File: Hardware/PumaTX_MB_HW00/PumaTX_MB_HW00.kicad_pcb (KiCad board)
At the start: 2 copper layers, 107 parts, among them J100 FH12A-26S-0.5SH_55_, J101 FH12-12S-0.5SH_55_, J102 500334-0160, J103 500334-0160, J104 692122030100, J105 53398-0667, J300 U.FL-R-SMT-1_40_, J410 U.FL-R-SMT-1_40_, M130 Motor_DC, M140 Fan, Q130 ZXMN3B01F, Q140 ZXMN3B01F, Q200 UMH3NTN, Q201 UMH3NTN, U200 CP2105-F01-GMR, U300 ESP32-PICO-D4, U400 ESP32-PICO-D4, U402 E28-2G4M27S, U410 SX1280, U500 BQ24075RGTR, U510 MIC5528-3.3YMT-T5, U520 MIC5528-3.3YMT-T5, U530 MIC5528-3.3YMT-T5, Y410 NX2016SA-52MHZ-EXS00A-CS06016

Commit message: Generated BOM and changed 2 capa footprints
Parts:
- C350, C450: footprint Capacitor_SMD:C_0402_1005Metric -> Capacitor_SMD:C_0603_1608Metric
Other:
- board outline added: 216 x 107.5 mm
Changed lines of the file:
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@@
     )
   )
-  (footprint "Capacitor_SMD:C_0402_1005Metric" (layer "F.Cu")
+  (footprint "Capacitor_SMD:C_0603_1608Metric" (layer "F.Cu")
     (at 145.52 80.08)
-    (descr "Capacitor SMD 0402 (1005 Metric), square (rectangular) end terminal, IPC_7351 nominal, (Body size source: IPC-SM-782 page 76, https://www.pcb-3d.com/wordpress/wp-content/uploads/ipc-sm-782a_amendment_1_and_2.pdf), generated with kicad-footprint-generator")
-    (tags "capacitor")
-    (property "Sheetfile" "PumaTX_MB_HW00.kicad_sch")
-    (property "Sheetname" "")
-    (attr smd)
-    (fp_text reference "C350" (at 0 -1.16) (layer "F.SilkS")
-      (effects (font (size 1 1) (thickness 0.15)))
-    )
-    (fp_text value "100n" (at 0 1.16) (layer "F.Fab")
-      (effects (font (size 1 1) (thickness 0.15)))
-    )
-    (fp_text user "${REFERENCE}" (at 0 0) (layer "F.Fab")
-      (effects (font (size 0.25 0.25) (thickness 0.04)))
-    )
-    (fp_line (start -0.107836 -0.36) (end 0.107836 -0.36) (layer "F.SilkS") (width 0.12))
-    (fp_line (start -0.107836 0.36) (end 0.107836 0.36) (layer "F.SilkS") (width 0.12))
-    (fp_line (start 0.91 -0.46) (end 0.91 0.46) (layer "F.CrtYd") (width 0.05))
-    (fp_line (start -0.91 -0.46) (end 0.91 -0.46) (layer "F.CrtYd") (width 0.05))
-    (fp_line (start 0.91 0.46) (end -0.91 0.46) (layer "F.CrtYd") (width 0.05))
-    (fp_line (start -0.91 0.46) (end -0.91 -0.46) (layer "F.CrtYd") (width 0.05))
-    (fp_line (start -0.5 -0.25) (end 0.5 -0.25) (layer "F.Fab") (width 0.1))
-    (fp_line (start -0.5 0.25) (end -0.5 -0.25) (layer "F.Fab") (width 0.1))
-    (fp_line (start 0.5 -0.25) (end 0.5 0.25) (layer "F.Fab") (width 0.1))
-    (fp_line (start 0.5 0.25) (end -0.5 0.25) (layer "F.Fab") (width 0.1))
-    (pad "1" smd roundrect (at -0.48 0) (size 0.56 0.62) (layers "F.Cu" "F.Paste" "F.Mask") (roundrect_rratio 0.25)
+    (descr "Capacitor SMD 0603 (1608 Metric), square (rectangular) end terminal, IPC_7351 nominal, (Body size source: IPC-SM-782 page 76, https://www.pcb-3d.com/wordpress/wp-content/uploads/ipc-sm-782a_amendment_1_and_2.pdf), generated with kicad-footprint-generator")
+    (tags "capacitor")
+    (property "Sheetfile" "PumaTX_MB_HW00.kicad_sch")
+    (property "Sheetname" "")
+    (attr smd)
+    (fp_text reference "C350" (at 0 -1.43) (layer "F.SilkS")
+      (effects (font (size 1 1) (thickness 0.15)))
+    )
+    (fp_text value "100n" (at 0 1.43) (layer "F.Fab")
+      (effects (font (size 1 1) (thickness 0.15)))
+    )
+    (fp_text user "${REFERENCE}" (at 0 0) (layer "F.Fab")
+      (effects (font (size 0.4 0.4) (thickness 0.06)))
+    )
+    (fp_line (start -0.14058 0.51) (end 0.14058 0.51) (layer "F.SilkS") (width 0.12))
+    (fp_line (start -0.14058 -0.51) (end 0.14058 -0.51) (layer "F.SilkS") (width 0.12))
+    (fp_line (start -1.48 -0.73) (end 1.48 -0.73) (layer "F.CrtYd") (width 0.05))
+    (fp_line (start -1.48 0.73) (end -1.48 -0.73) (layer "F.CrtYd") (width 0.05))
+    (fp_line (start 1.48 0.73) (end -1.48 0.73) (layer "F.CrtYd") (width 0.05))
+    (fp_line (start 1.48 -0.73) (end 1.48 0.73) (layer "F.CrtYd") (width 0.05))
+    (fp_line (start 0.8 0.4) (end -0.8 0.4) (layer "F.Fab") (width 0.1))
+    (fp_line (start -0.8 0.4) (end -0.8 -0.4) (layer "F.Fab") (width 0.1))
+    (fp_line (start -0.8 -0.4) (end 0.8 -0.4) (layer "F.Fab") (width 0.1))
+    (fp_line (start 0.8 -0.4) (end 0.8 0.4) (layer "F.Fab") (width 0.1))
+    (pad "1" smd roundrect (at -0.775 0) (size 0.9 0.95) (layers "F.Cu" "F.Paste" "F.Mask") (roundrect_rratio 0.25)
       (net 2 "+3V3") (pintype "passive"))
-    (pad "2" smd roundrect (at 0.48 0) (size 0.56 0.62) (layers "F.Cu" "F.Paste" "F.Mask") (roundrect_rratio 0.25)
-      (net 1 "GND") (pintype "passive"))
-    (model "${KICAD6_3DMODEL_DIR}/Capacitor_SMD.3dshapes/C_0402_1005Metric.wrl"
+    (pad "2" smd roundrect (at 0.775 0) (size 0.9 0.95) (layers "F.Cu" "F.Paste" "F.Mask") (roundrect_rratio 0.25)
+      (net 1 "GND") (pintype "passive"))
+    (model "${KICAD6_3DMODEL_DIR}/Capacitor_SMD.3dshapes/C_0603_1608Metric.wrl"
       (offset (xyz 0 0 0))
       (scale (xyz 1 1 1))
@@
     )
   )
-  (footprint "Capacitor_SMD:C_0402_1005Metric" (layer "F.Cu")
+  (footprint "Capacitor_SMD:C_0603_1608Metric" (layer "F.Cu")
     (at 142.65 77.47)
-    (descr "Capacitor SMD 0402 (1005 Metric), square (rectangular) end terminal, IPC_7351 nominal, (Body size source: IPC-SM-782 page 76, https://www.pcb-3d.com/wordpress/wp-content/uploads/ipc-sm-782a_amendment_1_and_2.pdf), generated with kicad-footprint-generator")
-    (tags "capacitor")
-    (property "Sheetfile" "PumaTX_MB_HW00.kicad_sch")
-    (property "Sheetname" "")
-    (attr smd)
-    (fp_text reference "C450" (at 0 -1.16) (layer "F.SilkS")
-      (effects (font (size 1 1) (thickness 0.15)))
-    )
-    (fp_text value "100n" (at 0 1.16) (layer "F.Fab")
-      (effects (font (size 1 1) (thickness 0.15)))
-    )
-    (fp_text user "${REFERENCE}" (at 0 0) (layer "F.Fab")
-      (effects (font (size 0.25 0.25) (thickness 0.04)))
-    )
-    (fp_line (start -0.107836 0.36) (end 0.107836 0.36) (layer "F.SilkS") (width 0.12))
-    (fp_line (start -0.107836 -0.36) (end 0.107836 -0.36) (layer "F.SilkS") (width 0.12))
-    (fp_line (start 0.91 -0.46) (end 0.91 0.46) (layer "F.CrtYd") (width 0.05))
-    (fp_line (start 0.91 0.46) (end -0.91 0.46) (layer "F.CrtYd") (width 0.05))
-    (fp_line (start -0.91 -0.46) (end 0.91 -0.46) (layer "F.CrtYd") (width 0.05))
-    (fp_line (start -0.91 0.46) (end -0.91 -0.46) (layer "F.CrtYd") (width 0.05))
-    (fp_line (start -0.5 0.25) (end -0.5 -0.25) (layer "F.Fab") (width 0.1))
-    (fp_line (start -0.5 -0.25) (end 0.5 -0.25) (layer "F.Fab") (width 0.1))
-    (fp_line (start 0.5 -0.25) (end 0.5 0.25) (layer "F.Fab") (width 0.1))
-    (fp_line (start 0.5 0.25) (end -0.5 0.25) (layer "F.Fab") (width 0.1))
-    (pad "1" smd roundrect (at -0.48 0) (size 0.56 0.62) (layers "F.Cu" "F.Paste" "F.Mask") (roundrect_rratio 0.25)
+    (descr "Capacitor SMD 0603 (1608 Metric), square (rectangular) end terminal, IPC_7351 nominal, (Body size source: IPC-SM-782 page 76, https://www.pcb-3d.com/wordpress/wp-content/uploads/ipc-sm-782a_amendment_1_and_2.pdf), generated with kicad-footprint-generator")
+    (tags "capacitor")
+    (property "Sheetfile" "PumaTX_MB_HW00.kicad_sch")
+    (property "Sheetname" "")
+    (attr smd)
+    (fp_text reference "C450" (at 0 -1.43) (layer "F.SilkS")
+      (effects (font (size 1 1) (thickness 0.15)))
+    )
+    (fp_text value "100n" (at 0 1.43) (layer "F.Fab")
+      (effects (font (size 1 1) (thickness 0.15)))
+    )
+    (fp_text user "${REFERENCE}" (at 0 0) (layer "F.Fab")
+      (effects (font (size 0.4 0.4) (thickness 0.06)))
+    )
+    (fp_line (start -0.14058 0.51) (end 0.14058 0.51) (layer "F.SilkS") (width 0.12))
+    (fp_line (start -0.14058 -0.51) (end 0.14058 -0.51) (layer "F.SilkS") (width 0.12))
+    (fp_line (start -1.48 -0.73) (end 1.48 -0.73) (layer "F.CrtYd") (width 0.05))
+    (fp_line (start -1.48 0.73) (end -1.48 -0.73) (layer "F.CrtYd") (width 0.05))
+    (fp_line (start 1.48 -0.73) (end 1.48 0.73) (layer "F.CrtYd") (width 0.05))
+    (fp_line (start 1.48 0.73) (end -1.48 0.73) (layer "F.CrtYd") (width 0.05))
+    (fp_line (start 0.8 -0.4) (end 0.8 0.4) (layer "F.Fab") (width 0.1))
+    (fp_line (start -0.8 -0.4) (end 0.8 -0.4) (layer "F.Fab") (width 0.1))
+    (fp_line (start 0.8 0.4) (end -0.8 0.4) (layer "F.Fab") (width 0.1))
+    (fp_line (start -0.8 0.4) (end -0.8 -0.4) (layer "F.Fab") (width 0.1))
+    (pad "1" smd roundrect (at -0.775 0) (size 0.9 0.95) (layers "F.Cu" "F.Paste" "F.Mask") (roundrect_rratio 0.25)
       (net 40 "-3V3") (pintype "passive"))
-    (pad "2" smd roundrect (at 0.48 0) (size 0.56 0.62) (layers "F.Cu" "F.Paste" "F.Mask") (roundrect_rratio 0.25)
-      (net 1 "GND") (pintype "passive"))
-    (model "${KICAD6_3DMODEL_DIR}/Capacitor_SMD.3dshapes/C_0402_1005Metric.wrl"
+    (pad "2" smd roundrect (at 0.775 0) (size 0.9 0.95) (layers "F.Cu" "F.Paste" "F.Mask") (roundrect_rratio 0.25)
+      (net 1 "GND") (pintype "passive"))
+    (model "${KICAD6_3DMODEL_DIR}/Capacitor_SMD.3dshapes/C_0603_1608Metric.wrl"
       (offset (xyz 0 0 0))
       (scale (xyz 1 1 1))
@@
     )
   )
+  (gr_rect (start 53.5 64.5) (end 269.5 172) (layer "Edge.Cuts") (width 0.1) (fill none))
 )

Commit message: PCB layout is done, routing to go!
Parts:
- M130, U300, U400: moved to B.Cu
- moved ANT400 106.9 mm to (216.5, 43.3)
- moved C101 106.9 mm to (234.5, 63.3)
- moved C102 106.9 mm to (213.4, 83.2)
- moved C103 106.9 mm to (237.4, 63.3)
- moved C110 106.9 mm to (249.5, 78.3)
- moved C120 106.9 mm to (241.5, 75.8)
- moved C200 106.9 mm to (229.2, 39.0)
- moved C201 106.9 mm to (228.6, 34.0)
- moved C202 106.9 mm to (233.2, 34.0)
- moved C203 106.9 mm to (233.2, 36.6)
- moved C301 106.9 mm to (243.2, 57.6)
- moved C303 106.9 mm to (225.7, 91.4)
- moved C304 106.9 mm to (225.7, 93.3)
- moved C306 106.9 mm to (236.2, 39.3)
- moved C307 106.9 mm to (239.0, 39.3)
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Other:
- board size 216 x 107.5 mm -> 130 x 40 mm

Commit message: quick layout update
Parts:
- moved D200 114.8 mm to (115.1, 117.2)
- moved Q140 98.7 mm to (184.7, 115.0)
- moved D130 89.7 mm to (193.2, 112.1)
- moved M140 89.6 mm to (179.6, 114.5)
- moved ANT400 78.3 mm to (190.4, 117.2)
- moved U530 71.9 mm to (193.0, 108.2)
- moved D140 71.8 mm to (174.5, 116.7)
- moved Q130 69.6 mm to (202.9, 108.2)
- moved Y410 62.5 mm to (165.1, 92.6)
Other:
- copper layers 2 -> 4
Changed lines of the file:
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@@
 (kicad_pcb (version 20211014) (generator pcbnew)
   (general
-    (thickness 1.6)
+    (thickness 4.69)
   )
   (paper "A4")
   (layers
     (0 "F.Cu" signal)
+    (1 "In1.Cu" signal)
+    (2 "In2.Cu" signal)
     (31 "B.Cu" signal)
     (32 "B.Adhes" user "B.Adhesive")
@@
   )
   (setup
+    (stackup
+      (layer "F.SilkS" (type "Top Silk Screen"))
+      (layer "F.Paste" (type "Top Solder Paste"))
+      (layer "F.Mask" (type "Top Solder Mask") (thickness 0.01))
+      (layer "F.Cu" (type "copper") (thickness 0.035))
+      (layer "dielectric 1" (type "core") (thickness 1.51) (material "FR4") (epsilon_r 4.5) (loss_tangent 0.02))
+      (layer "In1.Cu" (type "copper") (thickness 0.035))
+      (layer "dielectric 2" (type "prepreg") (thickness 1.51) (material "FR4") (epsilon_r 4.5) (loss_tangent 0.02))
+      (layer "In2.Cu" (type "copper") (thickness 0.035))
+      (layer "dielectric 3" (type "core") (thickness 1.51) (material "FR4") (epsilon_r 4.5) (loss_tangent 0.02))
+      (layer "B.Cu" (type "copper") (thickness 0.035))
+      (layer "B.Mask" (type "Bottom Solder Mask") (thickness 0.01))
+      (layer "B.Paste" (type "Bottom Solder Paste"))
+      (layer "B.SilkS" (type "Bottom Silk Screen"))
+      (copper_finish "None")
+      (dielectric_constraints no)
+    )
     (pad_to_mask_clearance 0)
     (pcbplotparams
@@
   )
   (footprint "Component_lib:S1GHE" (layer "F.Cu")
-    (at 230.39 30.528)
+    (at 193.162 112.1)
     (descr "S1GHE-2")
     (tags "Diode")
@@
   )
   (footprint "Package_TO_SOT_SMD:SOT-23" (layer "F.Cu")
-    (at 224.015 41.865)
+    (at 202.8625 108.15)
     (descr "SOT, 3 Pin (https://www.jedec.org/system/files/docs/to-236h.pdf variant AB), generated with kicad-footprint-generator ipc_gullwing_generator.py")
     (tags "SOT TO_SOT_SMD")
@@
   )
   (footprint "Component_lib:S1GHE" (layer "F.Cu")
-    (at 205.91 52.138)
+    (at 174.491 116.65)
     (descr "S1GHE-2")
     (tags "Diode")
@@
   )
   (footprint "Component_lib:SM02B-SURS-TF" (layer "F.Cu")
-    (at 224.37 36.84)
+    (at 179.6 114.5)
     (property "Sheetfile" "PumaTX_MB_HW00.kicad_sch")
     (property "Sheetname" "")
@@
   )
   (footprint "Component_lib:SON40P120X120X60-7N-D" (layer "F.Cu")
-    (at 228.185 45.54)
+    (at 193 108.25)
     (descr "MIC5528-3.3YMT-T5   6pin")
     (tags "Integrated Circuit")
@@
   )
   (footprint "Package_TO_SOT_SMD:SOT-23" (layer "F.Cu")
-    (at 235.915 30.565)
+    (at 184.65 114.95)
     (descr "SOT, 3 Pin (https://www.jedec.org/system/files/docs/to-236h.pdf variant AB), generated with kicad-footprint-generator ipc_gullwing_generator.py")
     (tags "SOT TO_SOT_SMD")
@@
   )
   (footprint "Component_lib:ANTC3216X140N" (layer "F.Cu")
-    (at 216.525 43.335)
+    (at 190.4 117.15)
     (descr "2450AT18A100E")
     (tags "Antenna")
@@
   )
   (footprint "Component_lib:NX2016SA32MEXS00ACS06465" (layer "F.Cu")
-    (at 211.64 50.91)
+    (at 165.1 92.6)
     (descr "NX2016SA-32M-EXS00A-CS06465-2")
     (tags "Crystal or Oscillator")
@@
   )
   (footprint "Component_lib:SP0503BAHTG" (layer "F.Cu")
-    (at 205.15 46)
+    (at 115.1 117.15)
     (descr "SP0503BAHTG-1")
     (tags "TVS Diode (Uni-directional)")

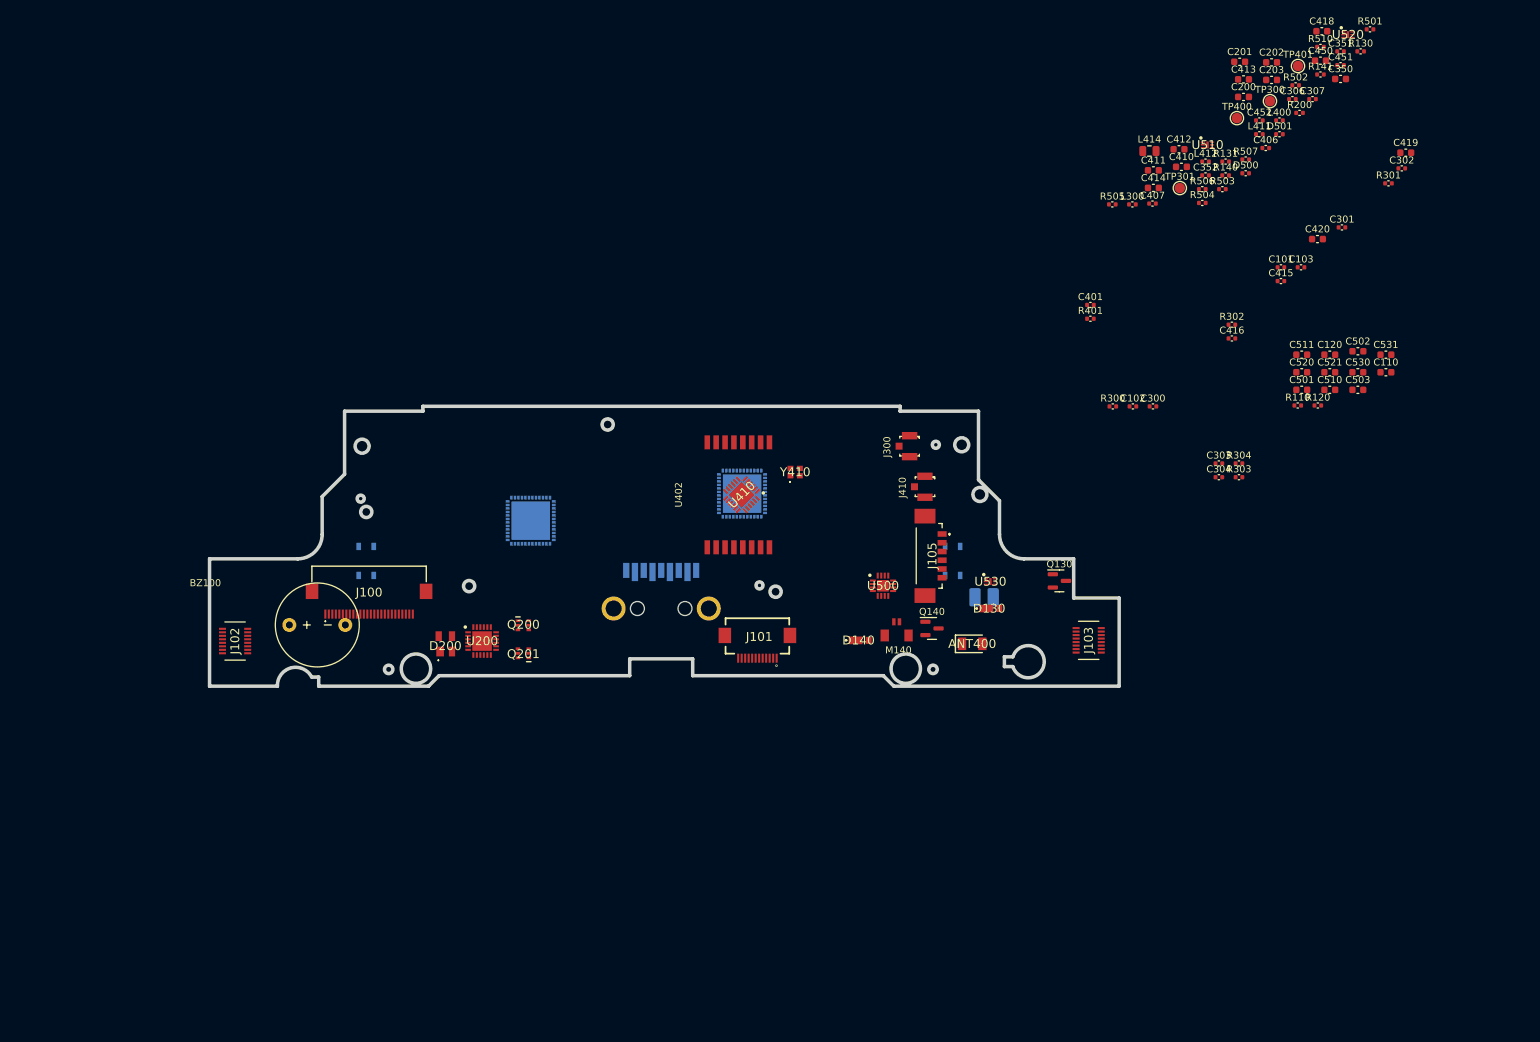
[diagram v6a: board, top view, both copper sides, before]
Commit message: Started layout
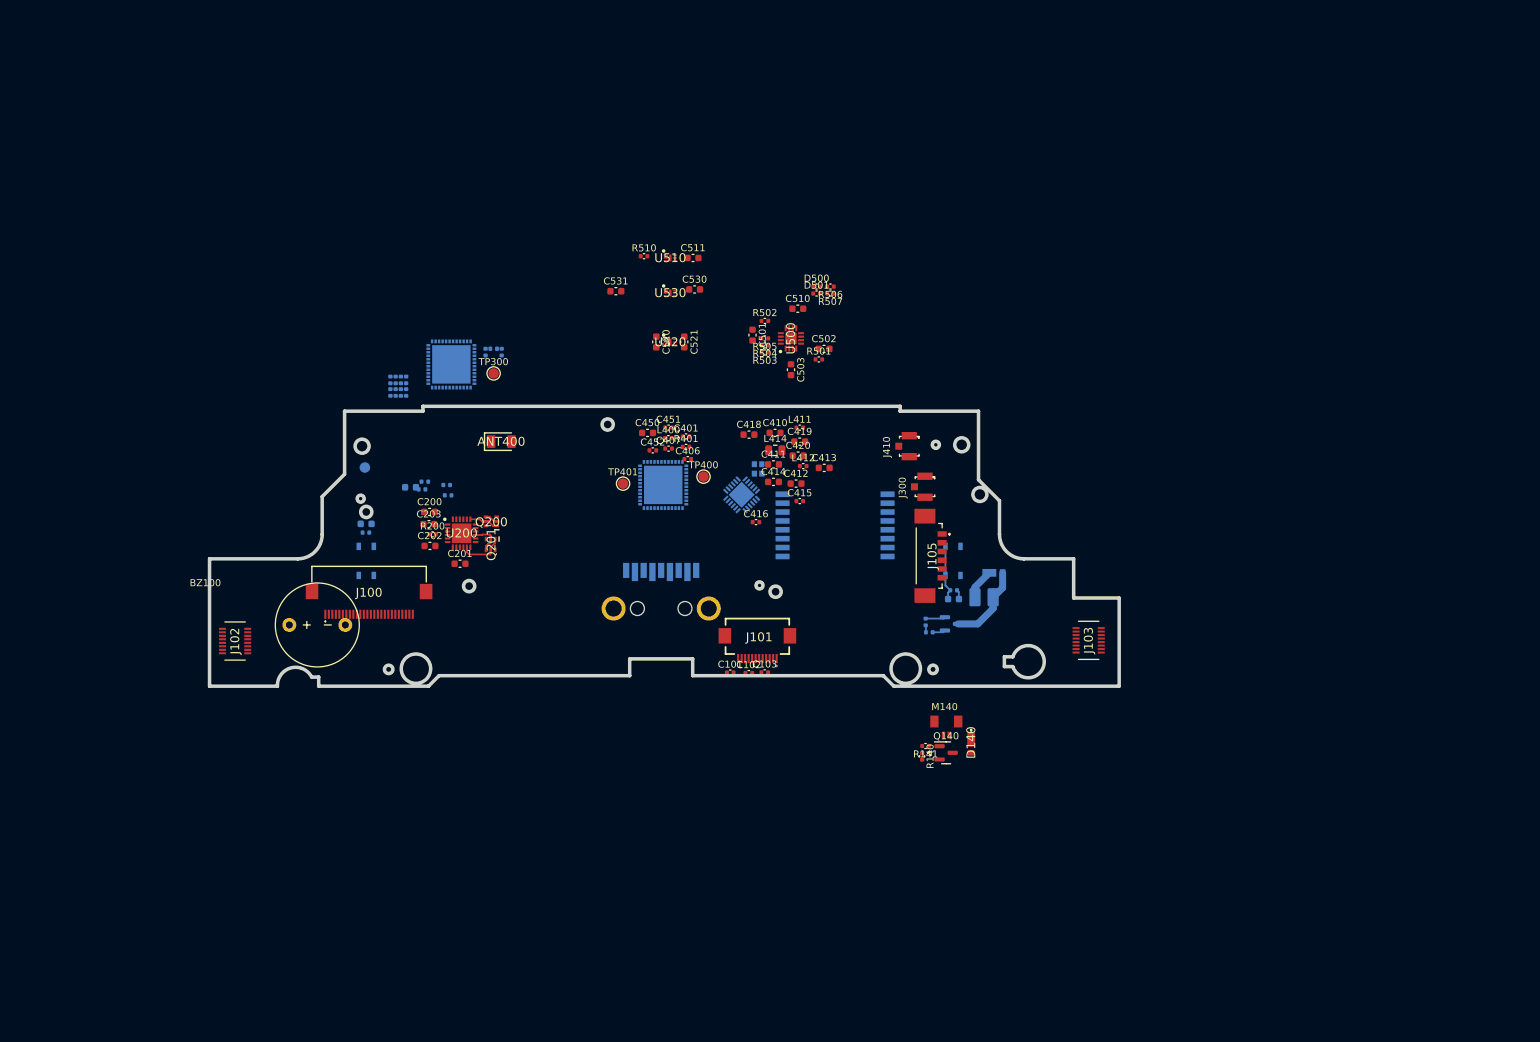
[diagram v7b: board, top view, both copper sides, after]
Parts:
- removed D200: SP0503BAHTG, Component_lib:SP0503BAHTG
- C110, C120, C300, C301, C302, C303, C304, C306, C307, C350, C351, C352, D130, L300, Q130, R110, R120, R130, R131, R300, R301, R302, R303, R304, TP301, U402, U410, Y410: moved to B.Cu
- moved C110 147.4 mm to (103.8, 100.0)
- moved C302 146.6 mm to (108.8, 81.2), turned to -90 degrees
- moved C351 145.4 mm to (111.8, 95.1), turned to 180 degrees
- moved C350 145.2 mm to (110.1, 94.8), turned to 180 degrees
- moved R301 144.6 mm to (108.0, 79.4), turned to -90 degrees
- moved C202 138.7 mm to (112.9, 103.2)
- moved R200 137.8 mm to (113.3, 101.5)
- moved C301 137.3 mm to (108.0, 81.2), turned to -90 degrees
- moved C203 136.1 mm to (112.8, 100.0)
- moved R110 134.4 mm to (103.8, 101.2)
- moved C201 132.5 mm to (117.2, 105.7)
- moved C200 130.6 mm to (112.8, 98.3)
- moved TP301 123.1 mm to (103.6, 92.0), turned to 180 degrees
- moved R304 121.9 mm to (107.2, 79.4), turned to -90 degrees
- moved C307 121.4 mm to (123.2, 75.5), turned to -90 degrees
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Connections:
- C502 pad 1: Net-(C502-Pad1) -> /VSYS
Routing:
- net /HAPTIC_LS: track 0.00 -> 11.6 mm
- net /C2: track 0.00 -> 7.95 mm
- net /ELRS_RTS: track 0.00 -> 6.66 mm
- net /ELRS_DTR: track 0.00 -> 4.69 mm
- net /HAPTIC_HS: track 0.00 -> 4.35 mm
- net /PUMATX_RTS: track 0.00 -> 4.17 mm
- net GND: track 0.00 -> 2.83 mm
- net /HAPTIC_G: track 0.00 -> 1.85 mm
- net /PUMATX_DTR: track 0.00 -> 1.82 mm
- net +3V3: track 0.00 -> 1.36 mm
- net /HAPTIC_PWM: track 0.00 -> 1.02 mm
